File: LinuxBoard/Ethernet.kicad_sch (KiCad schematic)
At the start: 31 parts, among them J1 Wuerth_7499010121A, U3 DP83848C, Y3 25MHz

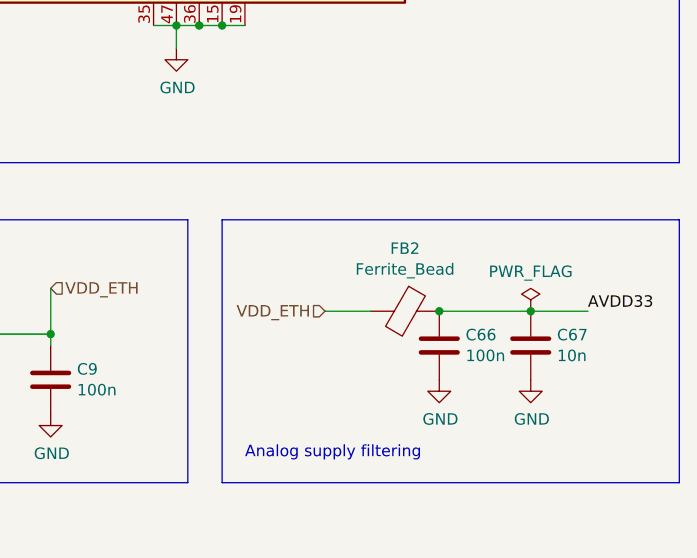
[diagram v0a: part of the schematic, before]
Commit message: Fix ERC errors and reorganize directory
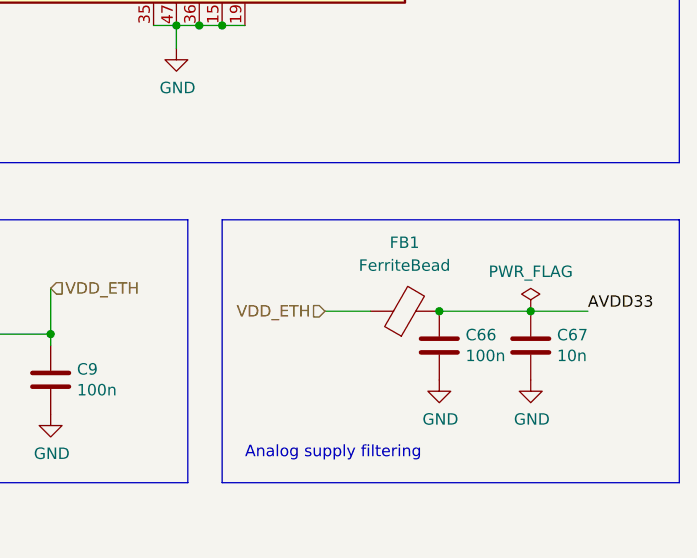
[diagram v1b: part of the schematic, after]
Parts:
- removed FB2: Ferrite_Bead, Inductor_SMD:L_0603_1608Metric, symbol Device:Ferrite_Bead
- added FB1: FerriteBead, Inductor_SMD:L_0603_1608Metric_Pad1.05x0.95mm_HandSolder, symbol Device:FerriteBead
- U3: footprint Package_QFP:LQFP-48-1EP_7x7mm_P0.5mm_EP3.6x3.6mm -> Package_QFP:LQFP-48_7x7mm_P0.5mm
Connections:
- net AVDD33: now also FB1.2
- net VDD_ETH: now also FB1.1
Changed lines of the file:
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@@
     (property "Reference" "U3" (id 0) (at 196.85 26.67 0))
     (property "Value" "DP83848C" (id 1) (at 198.12 30.48 0))
-    (property "Footprint" "Package_QFP:LQFP-48-1EP_7x7mm_P0.5mm_EP3.6x3.6mm" (id 2) (at 233.68 110.49 0)
+    (property "Footprint" "Package_QFP:LQFP-48_7x7mm_P0.5mm" (id 2) (at 233.68 110.49 0)
       (effects (font (size 1.27 1.27) italic) hide)
     )
@@
     (pin "1")
   )
-  (symbol (lib_id "Device:Ferrite_Bead") (at 231.14 143.51 270) (unit 1)
-    (in_bom yes) (on_board yes)
-    (property "Reference" "FB2" (id 0) (at 231.14 136.5504 90))
-    (property "Value" "Ferrite_Bead" (id 1) (at 231.14 138.8618 90))
-    (property "Footprint" "Inductor_SMD:L_0603_1608Metric" (id 2) (at 231.14 141.732 90)
-      (effects (font (size 1.27 1.27)) hide)
-    )
-    (property "Datasheet" "~" (id 3) (at 231.14 143.51 0)
-      (effects (font (size 1.27 1.27)) hide)
-    )
-    (pin "1")
-    (pin "2")
-  )
   (symbol (lib_id "Device:C") (at 234.95 147.32 0) (unit 1)
     (in_bom yes) (on_board yes)
@@
     (pin "1")
   )
+  (symbol (lib_id "Device:FerriteBead") (at 231.14 143.51 90) (unit 1)
+    (in_bom yes) (on_board yes) (fields_autoplaced)
+    (property "Reference" "FB1" (id 0) (at 231.0892 135.89 90))
+    (property "Value" "FerriteBead" (id 1) (at 231.0892 138.43 90))
+    (property "Footprint" "Inductor_SMD:L_0603_1608Metric_Pad1.05x0.95mm_HandSolder" (id 2) (at 231.14 145.288 90)
+      (effects (font (size 1.27 1.27)) hide)
+    )
+    (property "Datasheet" "~" (id 3) (at 231.14 143.51 0)
+      (effects (font (size 1.27 1.27)) hide)
+    )
+    (pin "1")
+    (pin "2")
+  )
 )

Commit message: Fix resistor footprints, restart layout
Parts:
- R10, R11, R12, R13, R16, R17, R9: footprint Resistor_SMD:R_0603_1608Metric -> Resistor_SMD:R_0603_1608Metric_Pad0.98x0.95mm_HandSolder
- R36, R6, R7, R8: footprint Resistor_SMD:R_0603_1608Metric_Pad1.05x0.95mm_HandSolder -> Resistor_SMD:R_0603_1608Metric_Pad0.98x0.95mm_HandSolder
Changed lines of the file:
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@@
     (property "Reference" "R9" (id 0) (at 138.43 38.1 0))
     (property "Value" "4.87K" (id 1) (at 139.7 35.56 0))
-    (property "Footprint" "Resistor_SMD:R_0603_1608Metric" (id 2) (at 136.398 35.56 90)
+    (property "Footprint" "Resistor_SMD:R_0603_1608Metric_Pad0.98x0.95mm_HandSolder" (id 2) (at 136.398 35.56 90)
       (effects (font (size 1.27 1.27)) hide)
     )
@@
       (effects (font (size 1.27 1.27)) (justify left))
     )
-    (property "Footprint" "Resistor_SMD:R_0603_1608Metric" (id 2) (at 120.142 35.56 90)
+    (property "Footprint" "Resistor_SMD:R_0603_1608Metric_Pad0.98x0.95mm_HandSolder" (id 2) (at 120.142 35.56 90)
       (effects (font (size 1.27 1.27)) hide)
     )
@@
       (effects (font (size 1.27 1.27)) (justify left))
     )
-    (property "Footprint" "Resistor_SMD:R_0603_1608Metric" (id 2) (at 123.952 35.56 90)
+    (property "Footprint" "Resistor_SMD:R_0603_1608Metric_Pad0.98x0.95mm_HandSolder" (id 2) (at 123.952 35.56 90)
       (effects (font (size 1.27 1.27)) hide)
     )
@@
       (effects (font (size 1.27 1.27)) (justify left))
     )
-    (property "Footprint" "Resistor_SMD:R_0603_1608Metric_Pad1.05x0.95mm_HandSolder" (id 2) (at 51.562 101.6 90)
+    (property "Footprint" "Resistor_SMD:R_0603_1608Metric_Pad0.98x0.95mm_HandSolder" (id 2) (at 51.562 101.6 90)
       (effects (font (size 1.27 1.27)) hide)
     )
@@
       (effects (font (size 1.27 1.27)) (justify left))
     )
-    (property "Footprint" "Resistor_SMD:R_0603_1608Metric_Pad1.05x0.95mm_HandSolder" (id 2) (at 51.562 111.76 90)
+    (property "Footprint" "Resistor_SMD:R_0603_1608Metric_Pad0.98x0.95mm_HandSolder" (id 2) (at 51.562 111.76 90)
       (effects (font (size 1.27 1.27)) hide)
     )
@@
       (effects (font (size 1.27 1.27)) (justify left))
     )
-    (property "Footprint" "Resistor_SMD:R_0603_1608Metric" (id 2) (at 70.612 101.6 90)
+    (property "Footprint" "Resistor_SMD:R_0603_1608Metric_Pad0.98x0.95mm_HandSolder" (id 2) (at 70.612 101.6 90)
       (effects (font (size 1.27 1.27)) hide)
     )
@@
       (effects (font (size 1.27 1.27)) (justify left))
     )
-    (property "Footprint" "Resistor_SMD:R_0603_1608Metric" (id 2) (at 70.612 111.76 90)
+    (property "Footprint" "Resistor_SMD:R_0603_1608Metric_Pad0.98x0.95mm_HandSolder" (id 2) (at 70.612 111.76 90)
       (effects (font (size 1.27 1.27)) hide)
     )
@@
       (effects (font (size 1.27 1.27)) (justify left))
     )
-    (property "Footprint" "Resistor_SMD:R_0603_1608Metric_Pad1.05x0.95mm_HandSolder" (id 2) (at 170.942 102.87 90)
+    (property "Footprint" "Resistor_SMD:R_0603_1608Metric_Pad0.98x0.95mm_HandSolder" (id 2) (at 170.942 102.87 90)
       (effects (font (size 1.27 1.27)) hide)
     )
@@
     (property "Reference" "R8" (id 0) (at 143.51 114.3 90))
     (property "Value" "0" (id 1) (at 140.97 114.3 90))
-    (property "Footprint" "Resistor_SMD:R_0603_1608Metric_Pad1.05x0.95mm_HandSolder" (id 2) (at 140.97 115.062 90)
+    (property "Footprint" "Resistor_SMD:R_0603_1608Metric_Pad0.98x0.95mm_HandSolder" (id 2) (at 140.97 115.062 90)
       (effects (font (size 1.27 1.27)) hide)
     )
@@
       (effects (font (size 1.27 1.27)) (justify left))
     )
-    (property "Footprint" "Resistor_SMD:R_0603_1608Metric" (id 2) (at 173.482 140.97 90)
+    (property "Footprint" "Resistor_SMD:R_0603_1608Metric_Pad0.98x0.95mm_HandSolder" (id 2) (at 173.482 140.97 90)
       (effects (font (size 1.27 1.27)) hide)
     )
@@
       (effects (font (size 1.27 1.27)) (justify left))
     )
-    (property "Footprint" "Resistor_SMD:R_0603_1608Metric" (id 2) (at 173.482 151.13 90)
-      (effects (font (size 1.27 1.27)) hide)
-    )
+    (property "Footprint" "Resistor_SMD:R_0603_1608Metric_Pad0.98x0.95mm_HandSolder" (id 2) (at 173.482 151.13 90)
+      (effects (font (size 1.27 1.27)) hide)
+    )
